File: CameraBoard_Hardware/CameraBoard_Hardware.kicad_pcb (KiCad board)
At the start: 2 copper layers, 61 x 99.3 mm, 38 parts, among them J1 BNC_75_OHM_HORIZ, J2 BNC_75_OHM_HORIZ, U1 TM4C129E_Launchpad, U2 OKI, U3 MAX4314ESD+, U4 MAX4314ESD+

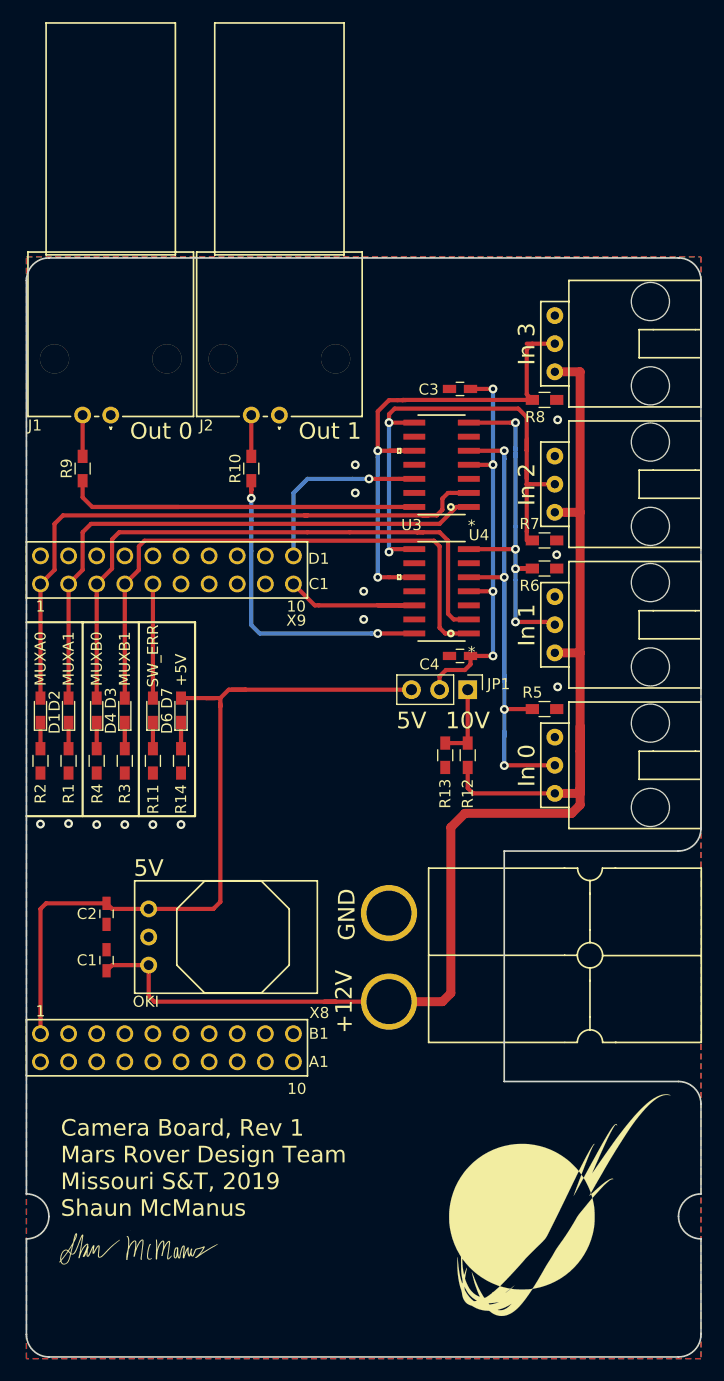
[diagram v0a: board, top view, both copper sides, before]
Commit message: Updated to Rev 2 Libraries
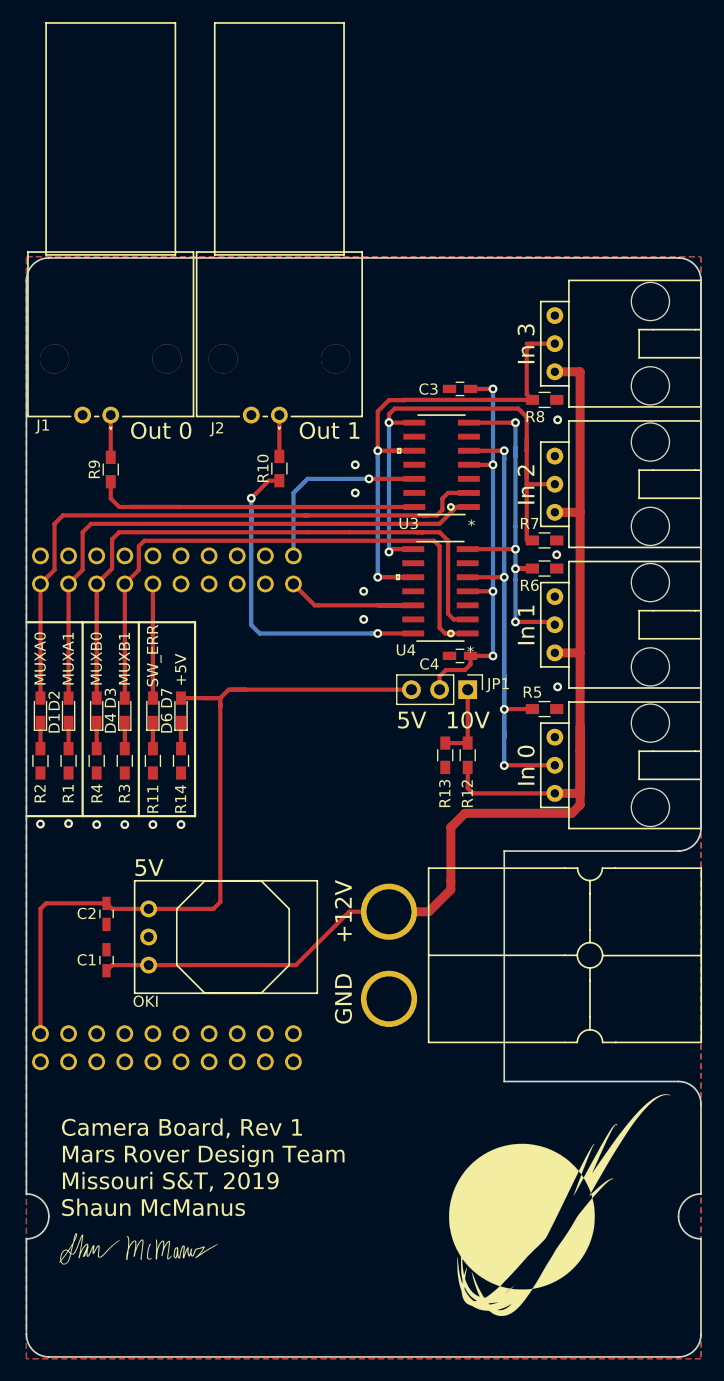
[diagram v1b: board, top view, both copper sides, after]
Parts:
- Conn1: footprint MRDT_Connectors:Anderson_2_Horisontal_Side_by_Side -> MRDT_Connectors:Anderson_2_Horizontal_Side_by_Side
- J1, J2: footprint BNC-75-Ohm-HORIZONTAL:BNC-75-Ohm-HORIZONTAL-1-1478032-0 -> MRDT_Connectors:BNC_THT_Horizontal
- U1: footprint MRDT_Shields:TM4C129E_Launchpad_X9_THT -> MRDT_Shields:TM4C129E_Launchpad_X9_THT_BOTTOM
- U3, U4: footprint MAX4314:MAX4314ESD&plus_ -> MRDT_ICs:MAX4314ESD+
- moved U3 5.00 mm to (125.9, 70.4)
- moved U4 4.96 mm to (125.8, 81.8)
- moved R9 2.54 mm to (94.0, 75.4)
- moved R10 2.54 mm to (109.2, 75.3)
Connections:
- J1 pad 1: GND -> Net-(J1-Pad1)
- J1 pad 2: Net-(J1-Pad2) -> GND
- J2 pad 1: GND -> Net-(J2-Pad1)
- J2 pad 2: Net-(J2-Pad2) -> GND
- R10 pad 2: Net-(J2-Pad2) -> Net-(J2-Pad1)
- R9 pad 2: Net-(J1-Pad2) -> Net-(J1-Pad1)
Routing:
- net +12V: track 127.5 -> 116.6 mm
- net Net-(J1-Pad1): track 0.00 -> 3.82 mm
- net Net-(J2-Pad2): track 3.73 -> 0.00 mm
- net Net-(J2-Pad1): track 0.00 -> 3.73 mm
- net Net-(J1-Pad2): track 3.73 -> 0.00 mm
- net CAM_OUT0: track 36.2 -> 33.8 mm
- net CAM_OUT1: track 29.9 -> 31.0 mm
